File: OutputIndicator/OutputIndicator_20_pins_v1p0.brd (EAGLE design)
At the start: 80 x 45 mm, 84 parts

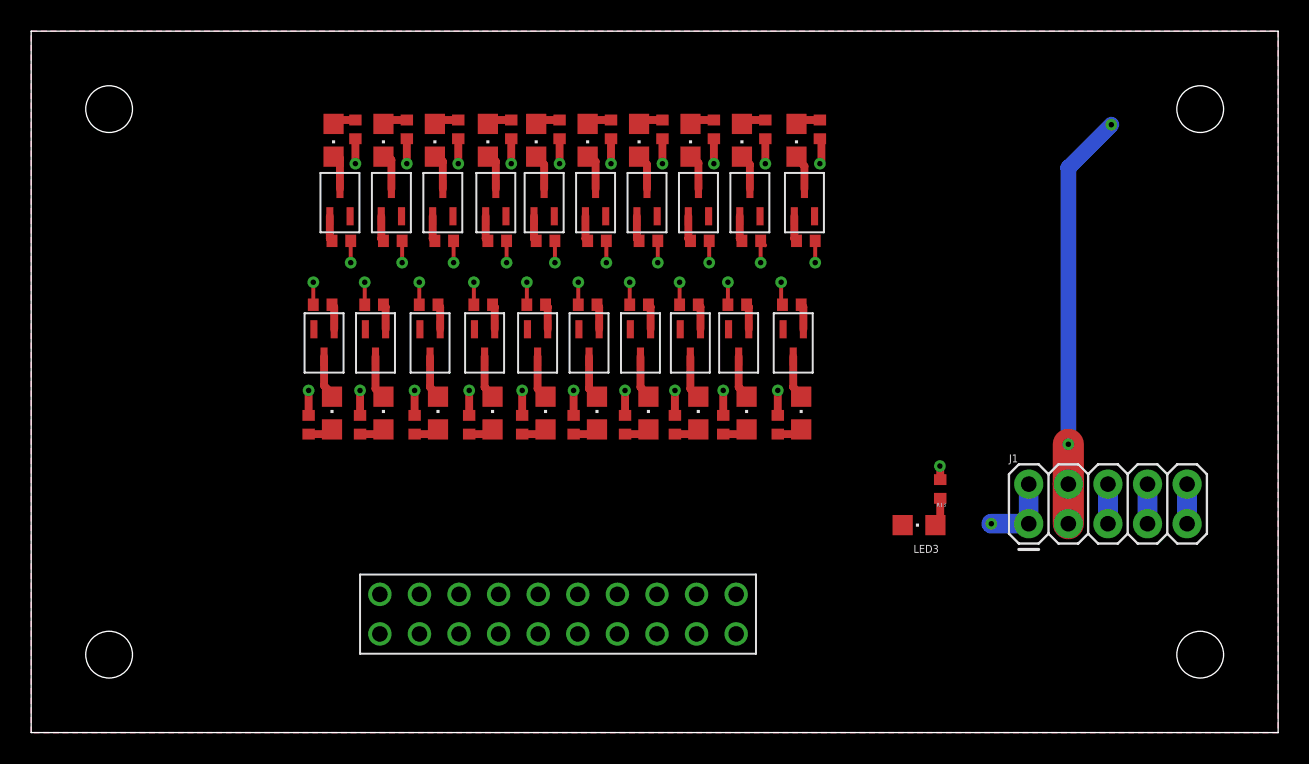
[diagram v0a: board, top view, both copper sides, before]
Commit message: Updated Design added Output to 20 pin header
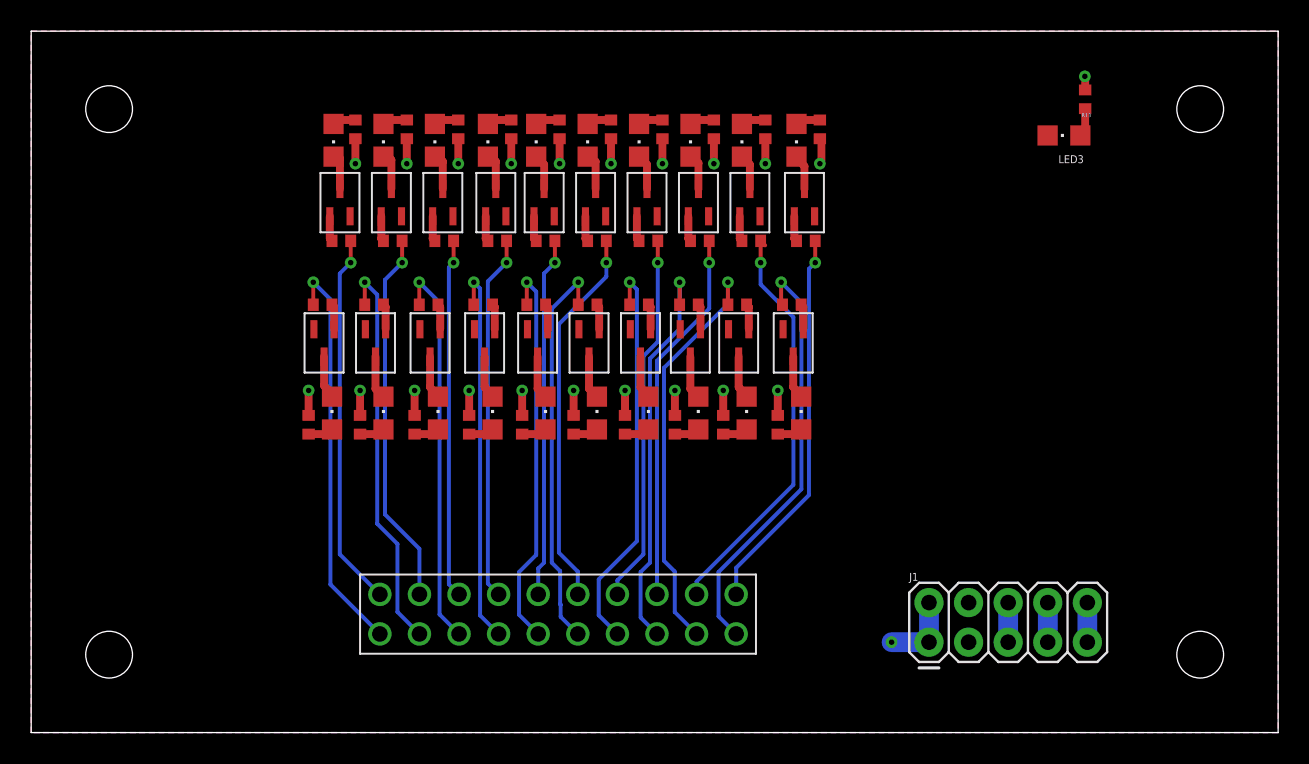
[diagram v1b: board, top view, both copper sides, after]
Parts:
- moved LED3 26.7 mm to (66.3, 38.3)
- moved R13 26.7 mm to (67.6, 40.6)
- moved J1 9.94 mm to (57.6, 5.80)
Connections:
- removed net IIC_1_SCL: RYS44.P$1
- removed net IIC_1_SDA: RYS3.P$1
- removed net INT_MI_03: RYS48.P$1
- removed net INT_MI_04: RYS7.P$1
- removed net INT_MI_05: RYS40.P$1
- removed net P1_02: RYS46.P$1
- removed net P1_03: RYS5.P$1
- removed net P1_06: RYS50.P$1
- removed net P1_07: RYS10.P$1
- removed net P6_00: RYS52.P$1
- removed net P6_01: RYS12.P$1
- removed net P6_02: RYS54.P$1
- removed net P6_03: RYS14.P$1
- removed net P6_04: RYS56.P$1
- removed net P6_05: RYS16.P$1
- removed net P6_06: RYS58.P$1
- removed net P6_07: RYS18.P$1
- removed net P8_00: RYS2.P$1
- removed net P8_01: RYS42.P$1
- removed net P8_02: RYS1.P$1
- new net P1: J2.P$1, RYS40.P$1
- new net P10: J2.P$10, RYS7.P$1
- new net P11: J2.P$11, RYS50.P$1
- new net P12: J2.P$12, RYS10.P$1
- new net P13: J2.P$13, RYS52.P$1
- new net P14: J2.P$14, RYS12.P$1
- new net P15: J2.P$15, RYS54.P$1
- new net P16: J2.P$16, RYS14.P$1
- new net P17: J2.P$17, RYS56.P$1
- new net P18: J2.P$18, RYS16.P$1
- new net P19: J2.P$19, RYS58.P$1
- new net P2: J2.P$2, RYS1.P$1
- new net P20: J2.P$20, RYS18.P$1
- new net P3: J2.P$3, RYS42.P$1
- new net P4: J2.P$4, RYS2.P$1
- new net P5: J2.P$5, RYS44.P$1
- new net P6: J2.P$6, RYS3.P$1
- new net P7: J2.P$7, RYS46.P$1
- new net P8: J2.P$8, RYS5.P$1
- new net P9: J2.P$9, RYS48.P$1
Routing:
- net P19: track 0.00 -> 27.2 mm, vias 0 -> 1
- net VDD: track 59.5 -> 32.5 mm, vias 23 -> 21
- net P17: track 0.00 -> 26.6 mm, vias 0 -> 1
- net P18: track 0.00 -> 26.5 mm, vias 0 -> 1
- net P1: track 0.00 -> 25.8 mm, vias 0 -> 1
- net P15: track 0.00 -> 25.7 mm, vias 0 -> 1
- net P13: track 0.00 -> 25.7 mm, vias 0 -> 1
- net P3: track 0.00 -> 25.5 mm, vias 0 -> 1
- net P11: track 0.00 -> 25.4 mm, vias 0 -> 1
- net P9: track 0.00 -> 25.2 mm, vias 0 -> 1
- net P5: track 0.00 -> 25.1 mm, vias 0 -> 1
- net P20: track 0.00 -> 24.8 mm, vias 0 -> 1
- net P7: track 0.00 -> 24.7 mm, vias 0 -> 1
- net P12: track 0.00 -> 24.4 mm, vias 0 -> 1
- net P16: track 0.00 -> 24.1 mm, vias 0 -> 1
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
